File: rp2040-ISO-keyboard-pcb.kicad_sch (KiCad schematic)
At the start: 82 parts, among them J1 USB_C_Receptacle_USB2.0, J2 Conn_01x04, U1 SRV05-4, U2 RP2040, U3 IS313741A, U4 XC6206, U5 W25Q128JVS, Y1 12MHz

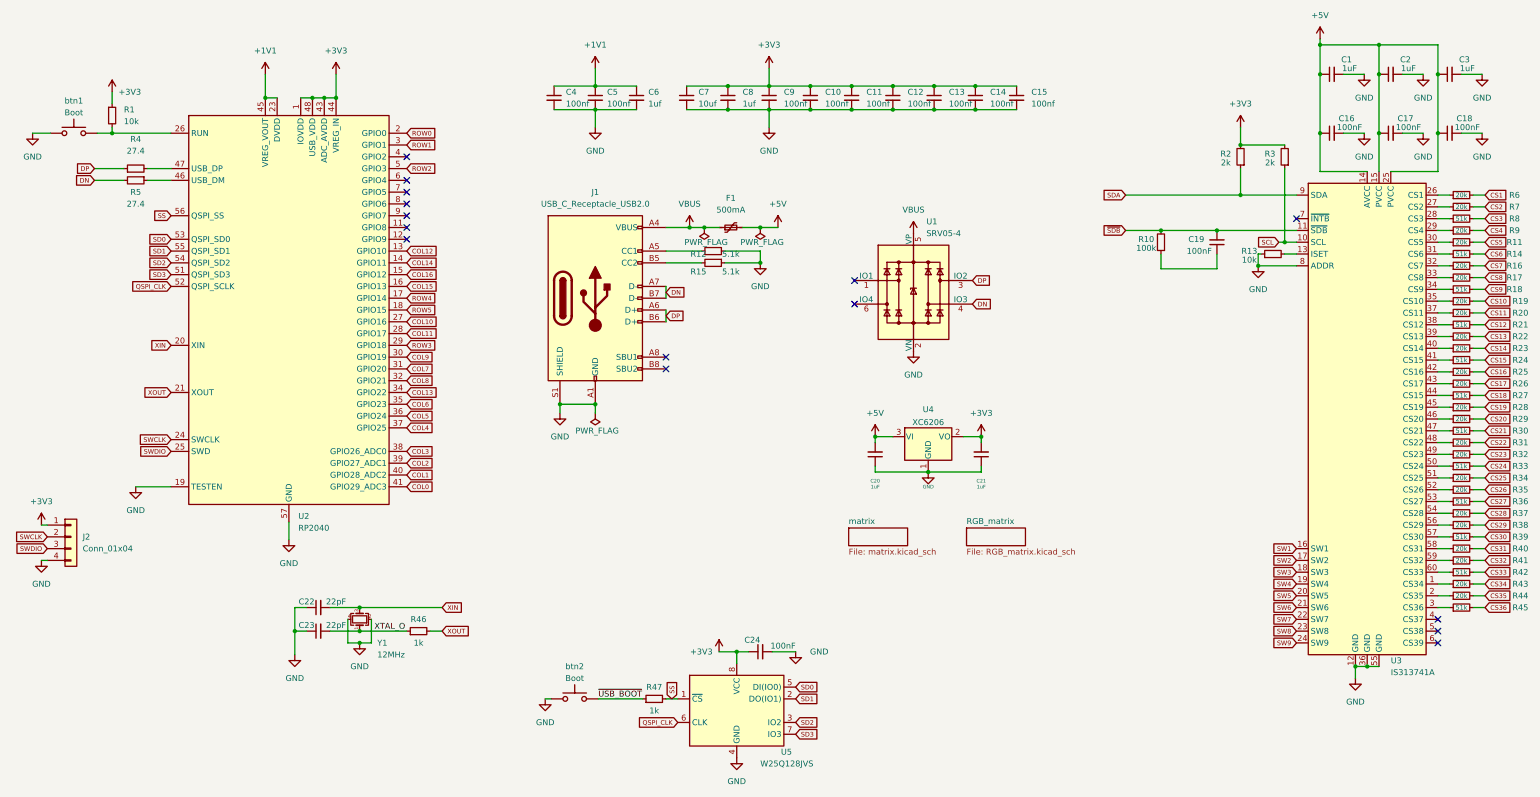
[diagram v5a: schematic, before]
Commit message: sw pins done
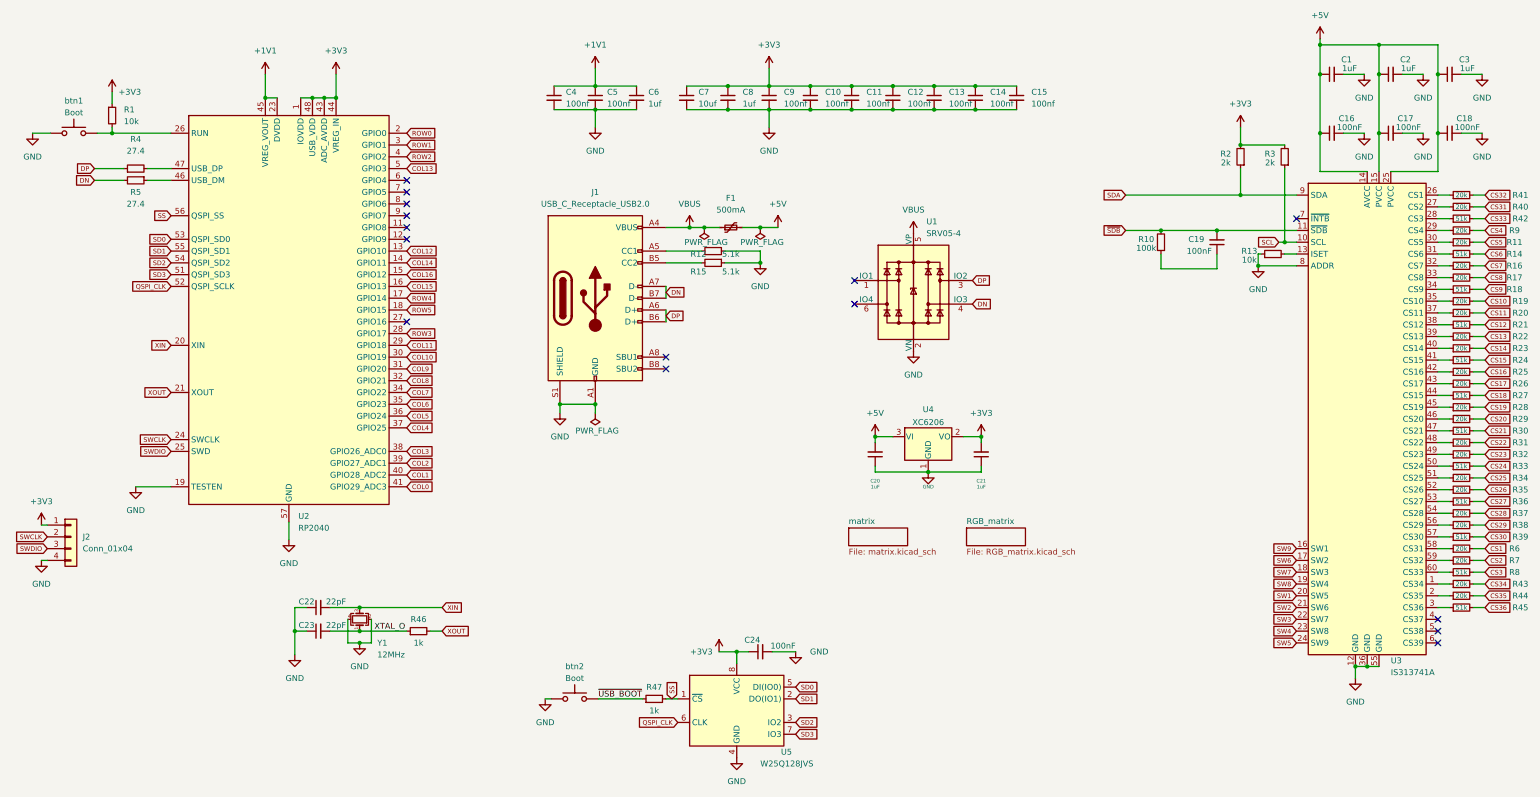
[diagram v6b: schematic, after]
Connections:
- net COL10: now also U2.30 (GPIO19); no longer U2.27 (GPIO16)
- net COL11: now also U2.29 (GPIO18); no longer U2.28 (GPIO17)
- net COL13: now also U2.5 (GPIO3); no longer U2.34 (GPIO22)
- net COL7: now also U2.34 (GPIO22); no longer U2.31 (GPIO20)
- net COL9: now also U2.31 (GPIO20); no longer U2.30 (GPIO19)
- net ROW2: now also U2.4 (GPIO2); no longer U2.5 (GPIO3)
- net ROW3: now also U2.28 (GPIO17); no longer U2.29 (GPIO18)
- net SW1: now also U3.20 (SW5); no longer U3.16 (SW1)
- net SW2: now also U3.21 (SW6); no longer U3.17 (SW2)
- net SW3: now also U3.22 (SW7); no longer U3.18 (SW3)
- net SW4: now also U3.23 (SW8); no longer U3.19 (SW4)
- net SW5: now also U3.24 (SW9); no longer U3.20 (SW5)
- net SW6: now also U3.17 (SW2); no longer U3.21 (SW6)
- net SW7: now also U3.18 (SW3); no longer U3.22 (SW7)
- net SW8: now also U3.19 (SW4); no longer U3.23 (SW8)
- net SW9: now also U3.16 (SW1); no longer U3.24 (SW9)
- net at R42.1: now also U3.28 (CS3); no longer U3.60 (CS33)
- net at R8.1: now also U3.60 (CS33); no longer U3.28 (CS3)
- net at R41.1: now also U3.26 (CS1); no longer U3.59 (CS32)
- net at R7.1: now also U3.59 (CS32); no longer U3.27 (CS2)
- net at R6.1: now also U3.58 (CS31); no longer U3.26 (CS1)
- net at R40.1: now also U3.27 (CS2); no longer U3.58 (CS31)
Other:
- moved on the sheet: R40, R41, R42, R6, R7, R8

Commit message: some more CS pins done
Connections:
- net at R20.1: now also U3.40 (CS14); no longer U3.37 (CS11)
- net at R14.1: now also U3.53 (CS27); no longer U3.31 (CS6)
- net at R21.1: now also U3.41 (CS15); no longer U3.38 (CS12)
- net at R9.1: now also U3.51 (CS25); no longer U3.29 (CS4)
- net at R29.1: now also U3.33 (CS8); no longer U3.46 (CS20)
- net at R22.1: now also U3.29 (CS4); no longer U3.39 (CS13)
- net at R36.1: now also U3.38 (CS12); no longer U3.53 (CS27)
- net at R17.1: now also U3.46 (CS20); no longer U3.33 (CS8)
- net at R24.1: now also U3.30 (CS5); no longer U3.41 (CS15)
- net at R35.1: now also U3.37 (CS11); no longer U3.52 (CS26)
- net at R23.1: now also U3.31 (CS6); no longer U3.40 (CS14)
- net at R30.1: now also U3.34 (CS9); no longer U3.47 (CS21)
- net at R16.1: now also U3.45 (CS19); no longer U3.32 (CS7)
- net at R18.1: now also U3.47 (CS21); no longer U3.34 (CS9)
- net at R28.1: now also U3.32 (CS7); no longer U3.45 (CS19)
- net at R19.1: now also U3.39 (CS13); no longer U3.35 (CS10)
- net at R34.1: now also U3.35 (CS10); no longer U3.51 (CS25)
- net at R11.1: now also U3.52 (CS26); no longer U3.30 (CS5)
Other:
- moved on the sheet: R11, R14, R16, R17, R18, R19, R20, R21, R22, R23, R24, R28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

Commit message: more routing
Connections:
- net at R26.1: now also U3.59 (CS32); no longer U3.43 (CS17)
- net at R20.1: now also U3.46 (CS20); no longer U3.40 (CS14)
- net at R21.1: now also U3.47 (CS21); no longer U3.41 (CS15)
- net at R25.1: now also U3.58 (CS31); no longer U3.42 (CS16)
- net at R17.1: now also U3.39 (CS13); no longer U3.46 (CS20)
- net at R8.1: now also U3.44 (CS15); no longer U3.60 (CS33)
- net at R16.1: now also U3.40 (CS14); no longer U3.45 (CS19)
- net at R7.1: now also U3.42 (CS16); no longer U3.59 (CS32)
- net at R6.1: now also U3.43 (CS17); no longer U3.58 (CS31)
- net at R18.1: now also U3.41 (CS15); no longer U3.47 (CS21)
- net at R27.1: now also U3.60 (CS33); no longer U3.44 (CS15)
- net at R19.1: now also U3.45 (CS19); no longer U3.39 (CS13)
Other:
- moved on the sheet: R16, R17, R18, R19, R20, R21, R25, R26, R27, R6, R7, R8
